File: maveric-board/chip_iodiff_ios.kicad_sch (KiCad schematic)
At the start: 1 part, among them U1 Socket

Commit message: add fmc lpc symbol
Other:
- title: (none) -> Maveric Board
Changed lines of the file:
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@@
 	(paper "A3")
 	(title_block
-		(date "2024-06-09")
+		(title "Maveric Board")
+		(date "2024-06-10")
 		(rev "0")
+		(comment 1 "Drawn By: Vighnesh Iyer")
 	)
 	(no_connect

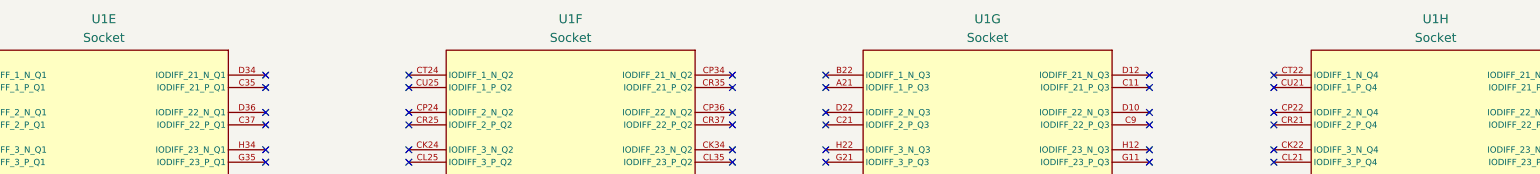
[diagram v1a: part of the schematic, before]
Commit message: reannotate, fix all ERCs
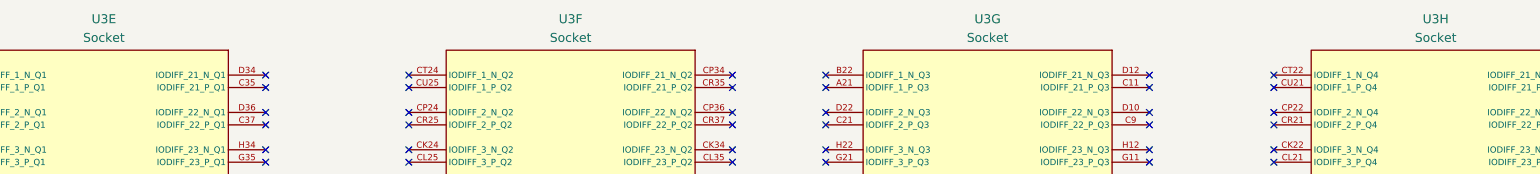
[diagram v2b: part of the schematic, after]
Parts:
- renumbered U1 to U3
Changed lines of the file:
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@@
 		(dnp no)
 		(fields_autoplaced yes)
-		(property "Reference" "U1"
+		(property "Reference" "U3"
 			(at 69.85 45.72 0)
 			(effects
@@
 			(project "maveric-board"
 				(path "/ae861d46-65fb-4872-932f-ad48addb0154/0a6f98c4-aa5e-45bf-95dd-7d1e294518d2"
-					(reference "U1")
+					(reference "U3")
 					(unit 5)
 				)
@@
 		(dnp no)
 		(fields_autoplaced yes)
-		(property "Reference" "U1"
+		(property "Reference" "U3"
 			(at 341.63 45.72 0)
 			(effects
@@
 			(project "maveric-board"
 				(path "/ae861d46-65fb-4872-932f-ad48addb0154/0a6f98c4-aa5e-45bf-95dd-7d1e294518d2"
-					(reference "U1")
+					(reference "U3")
 					(unit 8)
 				)
@@
 		(dnp no)
 		(fields_autoplaced yes)
-		(property "Reference" "U1"
+		(property "Reference" "U3"
 			(at 165.1 45.72 0)
 			(effects
@@
 			(project "maveric-board"
 				(path "/ae861d46-65fb-4872-932f-ad48addb0154/0a6f98c4-aa5e-45bf-95dd-7d1e294518d2"
-					(reference "U1")
+					(reference "U3")
 					(unit 6)
 				)
@@
 		(dnp no)
 		(fields_autoplaced yes)
-		(property "Reference" "U1"
+		(property "Reference" "U3"
 			(at 250.19 45.72 0)
 			(effects
@@
 			(project "maveric-board"
 				(path "/ae861d46-65fb-4872-932f-ad48addb0154/0a6f98c4-aa5e-45bf-95dd-7d1e294518d2"
-					(reference "U1")
+					(reference "U3")
 					(unit 7)
 				)

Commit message: add uni2 socket footprint, check against drawing, fix npth, assign all footprints and part numbers
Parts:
- U3: footprint (none) -> maveric-parts:BGA-1733-.92-47.725x47.725
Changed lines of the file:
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@@
 			)
 		)
-		(property "Footprint" ""
+		(property "Footprint" "maveric-parts:BGA-1733-.92-47.725x47.725"
 			(at 31.75 52.07 0)
 			(effects
@@
 			)
 		)
-		(property "Footprint" ""
+		(property "Footprint" "maveric-parts:BGA-1733-.92-47.725x47.725"
 			(at 303.53 52.07 0)
 			(effects
@@
 			)
 		)
-		(property "Footprint" ""
+		(property "Footprint" "maveric-parts:BGA-1733-.92-47.725x47.725"
 			(at 127 52.07 0)
 			(effects
@@
 			)
 		)
-		(property "Footprint" ""
+		(property "Footprint" "maveric-parts:BGA-1733-.92-47.725x47.725"
 			(at 212.09 52.07 0)
 			(effects

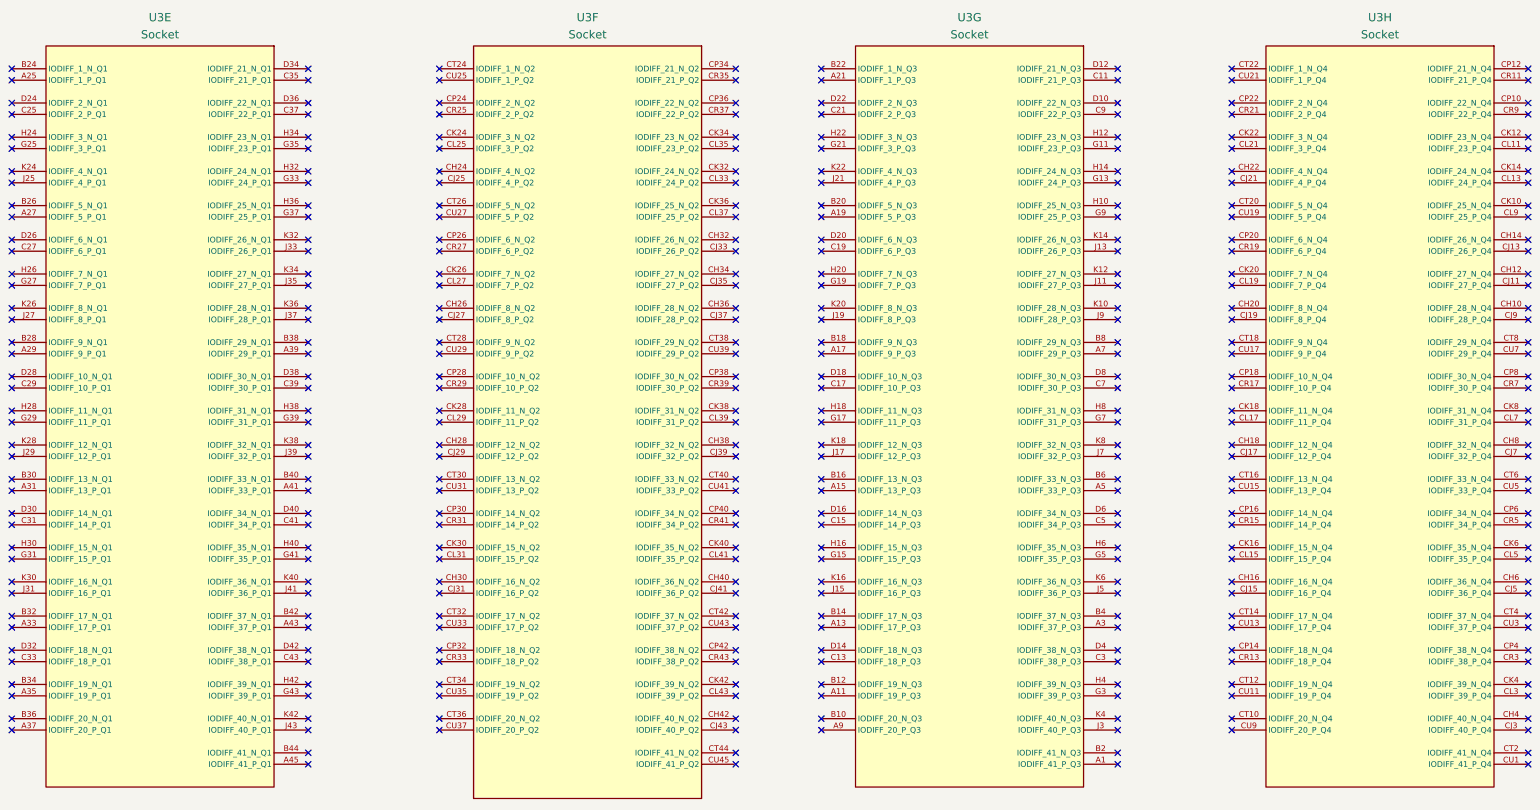
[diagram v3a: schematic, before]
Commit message: some docs + dnp uni2 socket
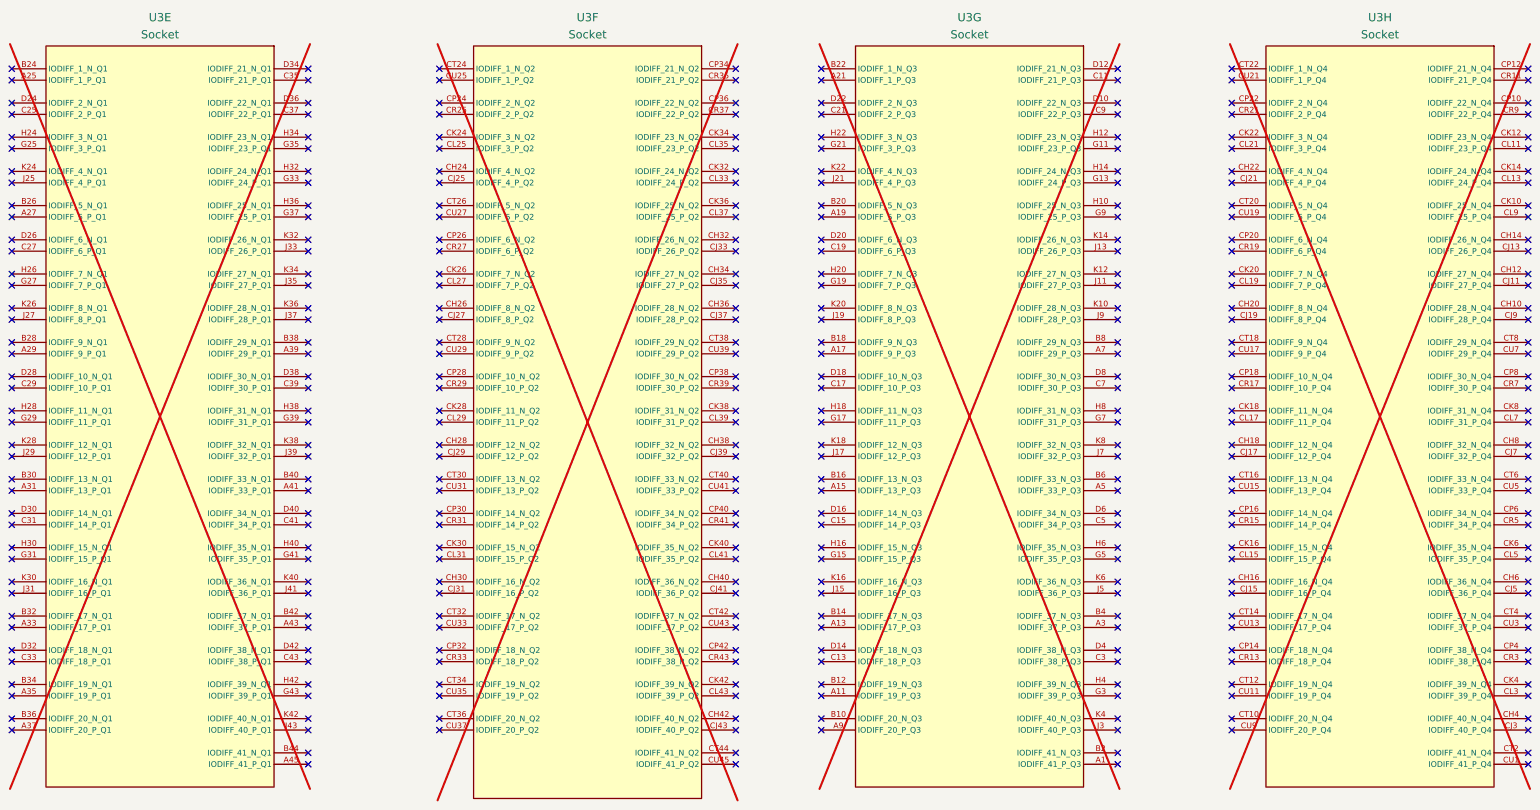
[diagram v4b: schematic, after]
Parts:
- U3: now not fitted
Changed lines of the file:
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@@
 		(in_bom yes)
 		(on_board yes)
-		(dnp no)
+		(dnp yes)
 		(fields_autoplaced yes)
 		(property "Reference" "U3"
@@
 		(in_bom yes)
 		(on_board yes)
-		(dnp no)
+		(dnp yes)
 		(fields_autoplaced yes)
 		(property "Reference" "U3"
@@
 		(in_bom yes)
 		(on_board yes)
-		(dnp no)
+		(dnp yes)
 		(fields_autoplaced yes)
 		(property "Reference" "U3"
@@
 		(in_bom yes)
 		(on_board yes)
-		(dnp no)
+		(dnp yes)
 		(fields_autoplaced yes)
 		(property "Reference" "U3"

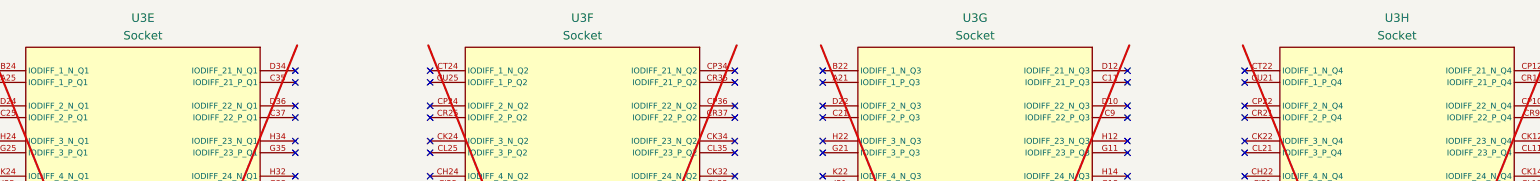
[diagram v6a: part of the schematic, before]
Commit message: fixup schematic + redo banana jack footprints to match jlc render
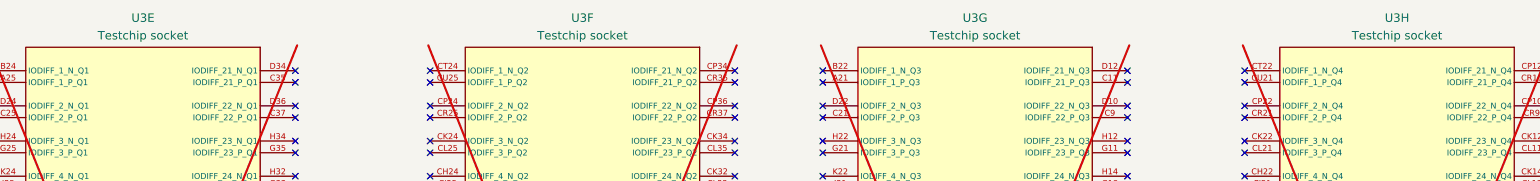
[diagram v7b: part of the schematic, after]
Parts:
- U3: value Socket -> Testchip socket
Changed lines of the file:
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@@
 			)
 		)
-		(property "Value" "Socket"
+		(property "Value" "Testchip socket"
 			(at 69.85 49.53 0)
 			(effects
@@
 			)
 		)
-		(property "Value" "Socket"
+		(property "Value" "Testchip socket"
 			(at 341.63 49.53 0)
 			(effects
@@
 			)
 		)
-		(property "Value" "Socket"
+		(property "Value" "Testchip socket"
 			(at 165.1 49.53 0)
 			(effects
@@
 			)
 		)
-		(property "Value" "Socket"
+		(property "Value" "Testchip socket"
 			(at 250.19 49.53 0)
 			(effects
